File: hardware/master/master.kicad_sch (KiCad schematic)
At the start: 45 parts, among them U1 ATtiny1604-SS, U2 esp32-wemos-d1-mini, U3 LOGIC_LEVEL_2CH_3V3_5V

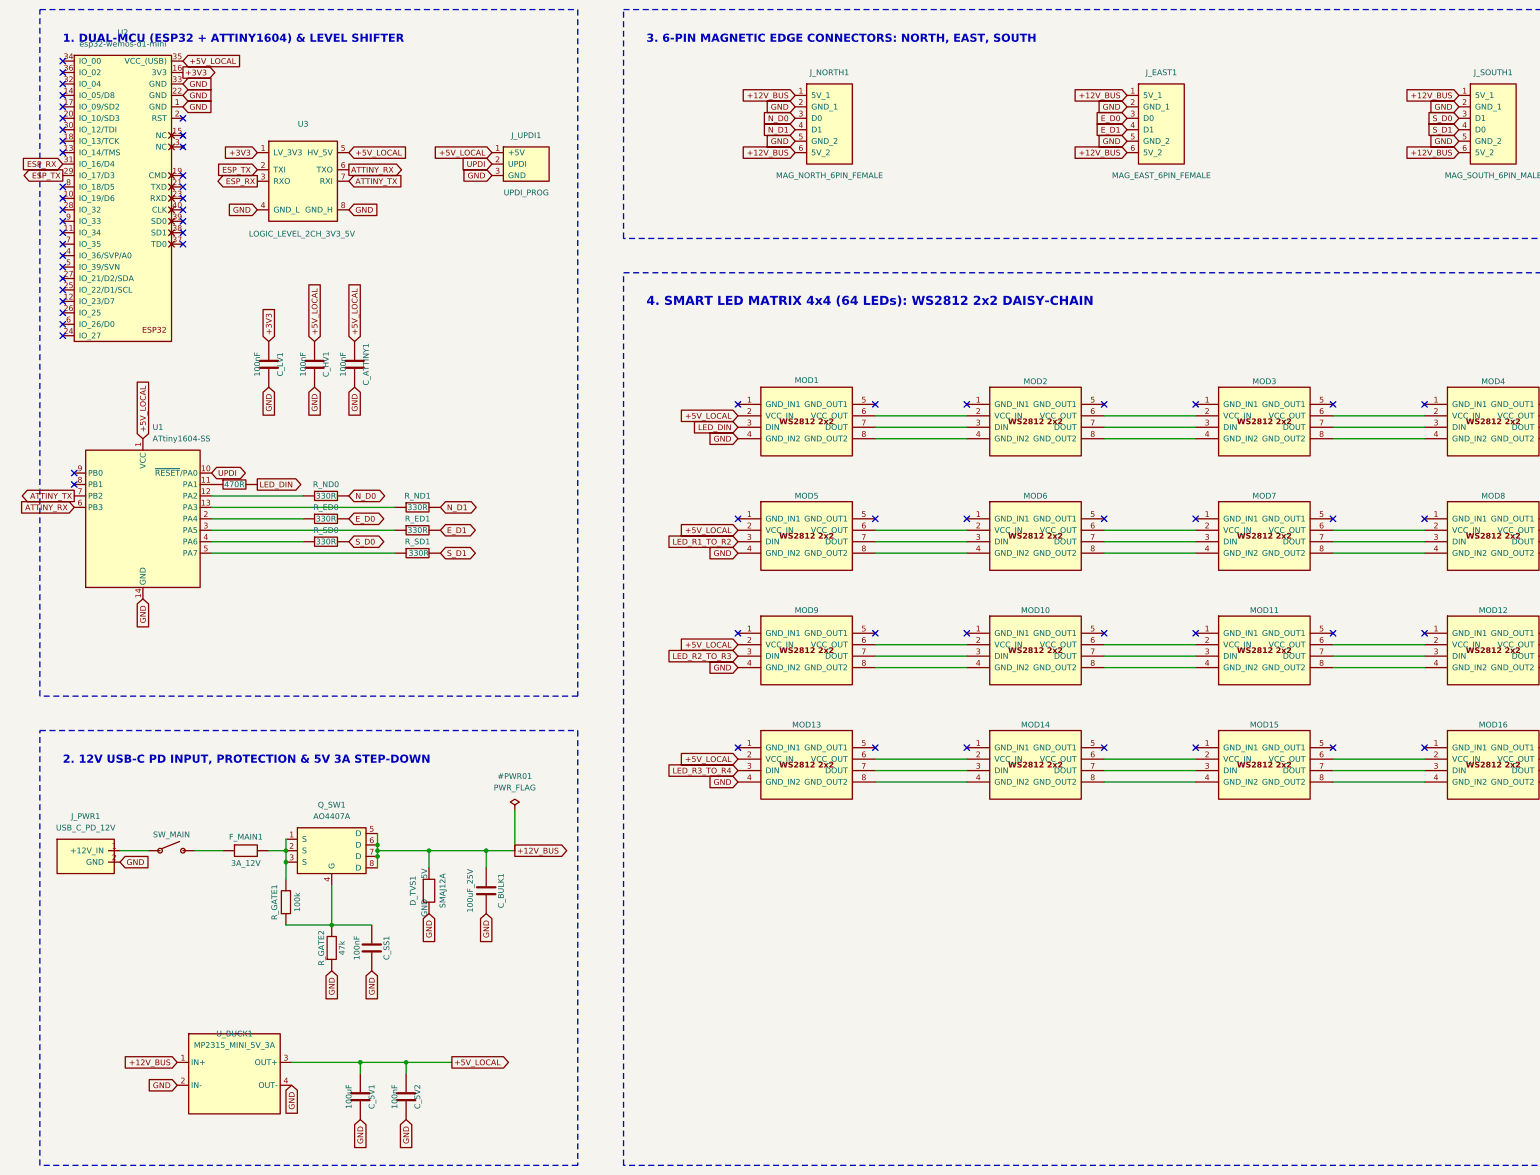
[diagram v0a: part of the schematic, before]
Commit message: feat(hardware): reorganize project structure, add master PCB, and update component libraries
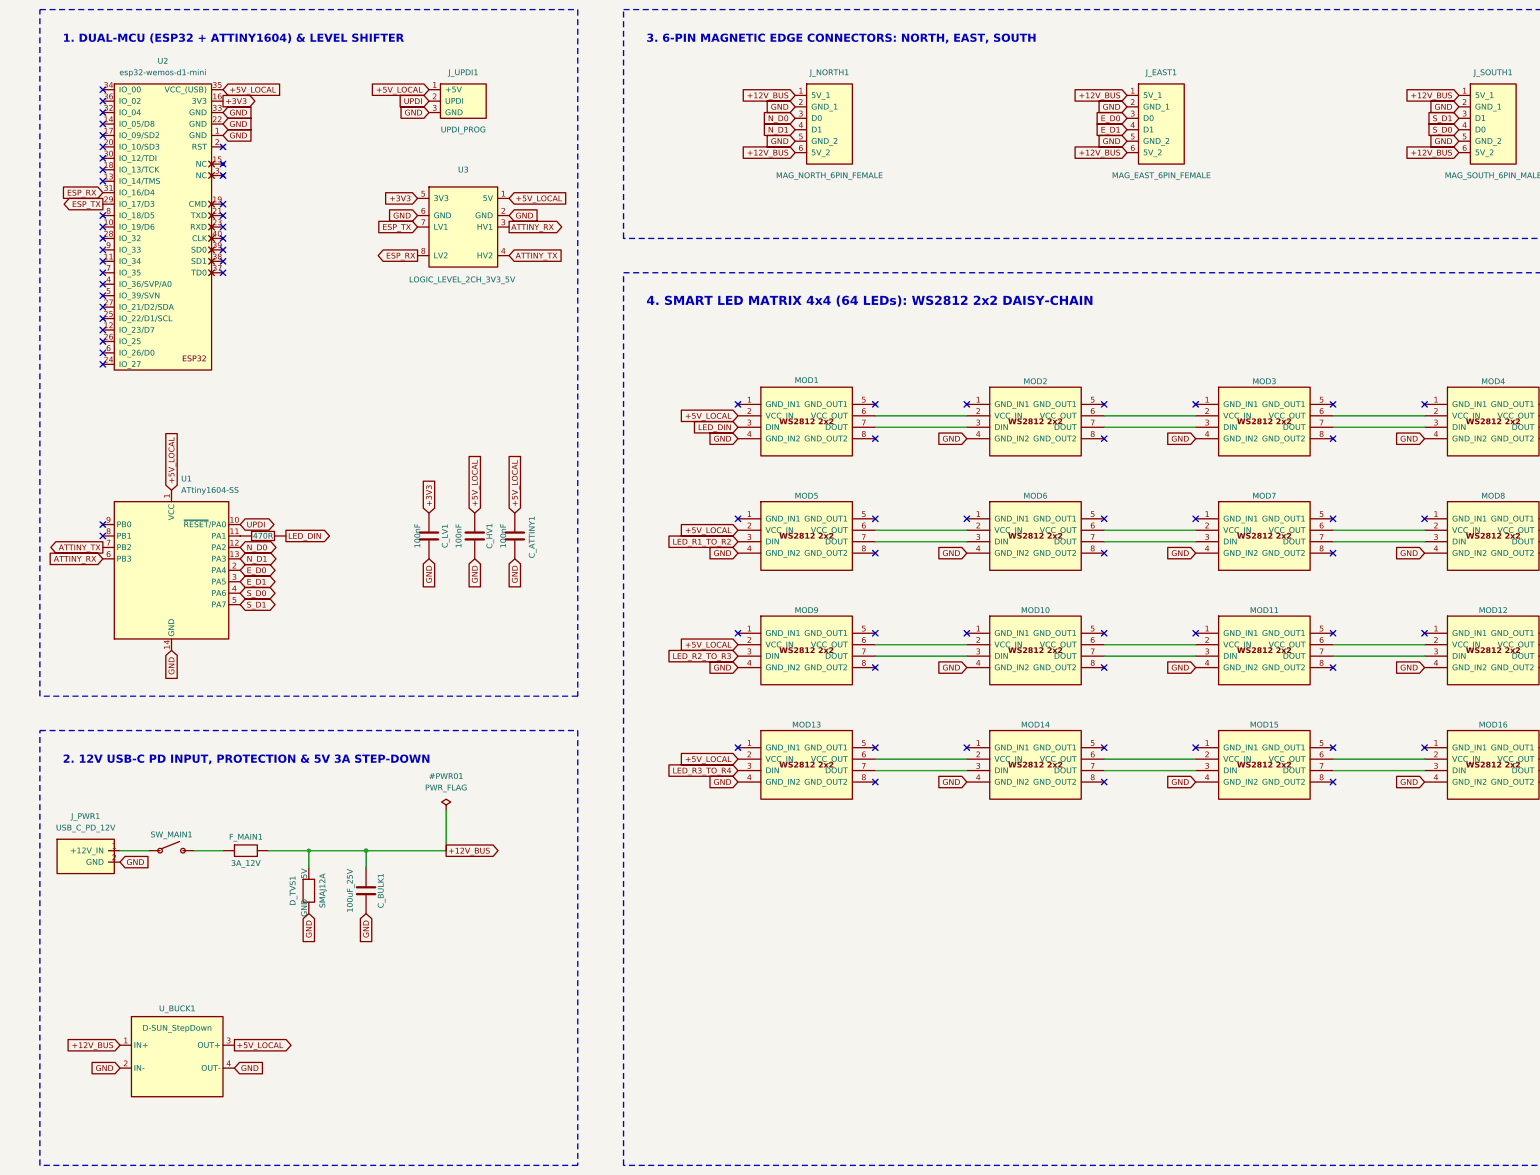
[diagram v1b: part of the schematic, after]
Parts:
- removed C_5V1: 100uF, symbol board_game:Capacitor
- removed C_5V2, C_SS1: 100nF, symbol board_game:Capacitor
- removed Q_SW1: AO4407A, symbol board_game:AO4407A
- removed R_ED0, R_ED1, R_ND0, R_ND1, R_SD0, R_SD1: 330R, Resistor_SMD:R_0603_1608Metric, symbol board_game:Series_Resistor
- removed R_GATE1: 100k, symbol board_game:Series_Resistor
- removed R_GATE2: 47k, symbol board_game:Series_Resistor
- C_BULK1: footprint (none) -> Capacitor_SMD:CP_Elec_6.3x7.7
- D_TVS1: footprint (none) -> Diode_SMD:D_SMA
- F_MAIN1: footprint (none) -> Fuse:Fuse_1206_3216Metric
- J_EAST1, J_NORTH1: footprint (none) -> magnetic-connector:fakemag6pin90degFemale
- J_PWR1: footprint Connector_USB:USB_C_Receptacle_HRO_TYPE-C-31-M-12 -> usb-c-pd-ip2721:usb-c-pd-ip2721
- J_SOUTH1: footprint (none) -> magnetic-connector:fakemag6pin90degMale
- J_UPDI1: footprint Connector_PinHeader_2.54mm:PinHeader_1x03_P2.54mm_Vertical -> pin-header-1x03-smd:pin-header-1x03-smd
- SW_MAIN1: renamed from SW_MAIN; value SW_SPST -> SW_JST_XH_2P; footprint (none) -> Connector_JST:JST_XH_B2B-XH-A_1x02_P2.50mm_Vertical
- U3: footprint (none) -> logic-level-converter-2ch:logic-level-converter-2ch
- U_BUCK1: value MP2315_MINI_5V_3A -> D-SUN_StepDown; footprint Module:MP2315_Mini_StepDown -> d-sun-stepdown:d-sun-stepdown; symbol board_game:MP2315_StepDown -> d-sun-stepdown:d-sun-stepdown
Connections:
- net +12V_BUS: now also F_MAIN1.2
- net +3V3: now also U3.5 (3V3); no longer U3.1 (LV_3V3)
- net +5V_LOCAL: now also U3.1 (5V); no longer U3.5 (HV_5V)
- net ATTINY_RX: now also U3.3 (HV1); no longer U3.6 (TXO)
- net ATTINY_TX: now also U3.4 (HV2); no longer U3.7 (RXI)
- net ESP_RX: now also U3.8 (LV2); no longer U3.3 (RXO)
- net ESP_TX: now also U3.7 (LV1); no longer U3.2 (TXI)
- net E_D0: now also U1.2 (PA4)
- net E_D1: now also U1.3 (PA5)
- net GND: now also MOD10.4 (GND_IN2), MOD11.4 (GND_IN2), MOD12.4 (GND_IN2), MOD14.4 (GND_IN2), MOD15.4 (GND_IN2), MOD16.4 (GND_IN2), MOD2.4 (GND_IN2), MOD3.4 (GND_IN2), MOD4.4 (GND_IN2), MOD6.4 (GND_IN2), MOD7.4 (GND_IN2), MOD8.4 (GND_IN2), U3.2 (GND), U3.6 (GND); no longer U3.4 (GND_L), U3.8 (GND_H)
- net N_D0: now also U1.12 (PA2)
- net N_D1: now also U1.13 (PA3)
- net S_D0: now also J_SOUTH1.4 (D0), U1.4 (PA6); no longer J_SOUTH1.3 (D1)
- net S_D1: now also J_SOUTH1.3 (D1), U1.5 (PA7); no longer J_SOUTH1.4 (D0)
- net at MOD15.8 (GND_OUT2): no longer MOD16.4 (GND_IN2)
- net at MOD1.8 (GND_OUT2): no longer MOD2.4 (GND_IN2)
- net at MOD6.8 (GND_OUT2): no longer MOD7.4 (GND_IN2)
- net at MOD7.8 (GND_OUT2): no longer MOD8.4 (GND_IN2)
- net at MOD9.8 (GND_OUT2): no longer MOD10.4 (GND_IN2)
- net at MOD10.8 (GND_OUT2): no longer MOD11.4 (GND_IN2)
- net at MOD2.8 (GND_OUT2): no longer MOD3.4 (GND_IN2)
- net at MOD3.8 (GND_OUT2): no longer MOD4.4 (GND_IN2)
- net at MOD14.8 (GND_OUT2): no longer MOD15.4 (GND_IN2)
- net at MOD5.8 (GND_OUT2): no longer MOD6.4 (GND_IN2)
- net at MOD11.8 (GND_OUT2): no longer MOD12.4 (GND_IN2)
- net at MOD13.8 (GND_OUT2): no longer MOD14.4 (GND_IN2)
- no-connect marks 76 -> 88
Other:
- moved on the sheet: C_ATTINY1, C_BULK1, C_HV1, C_LV1, D_TVS1, J_UPDI1, U1, U2, U3, U_BUCK1
